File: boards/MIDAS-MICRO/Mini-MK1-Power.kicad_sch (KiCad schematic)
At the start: 20 parts, among them J201 TestPoint, J202 Conn_01x02, U201 TVS1800DRV, U202 TVS1800DRV, U203 TPS2121, U204 TPS746-Q1

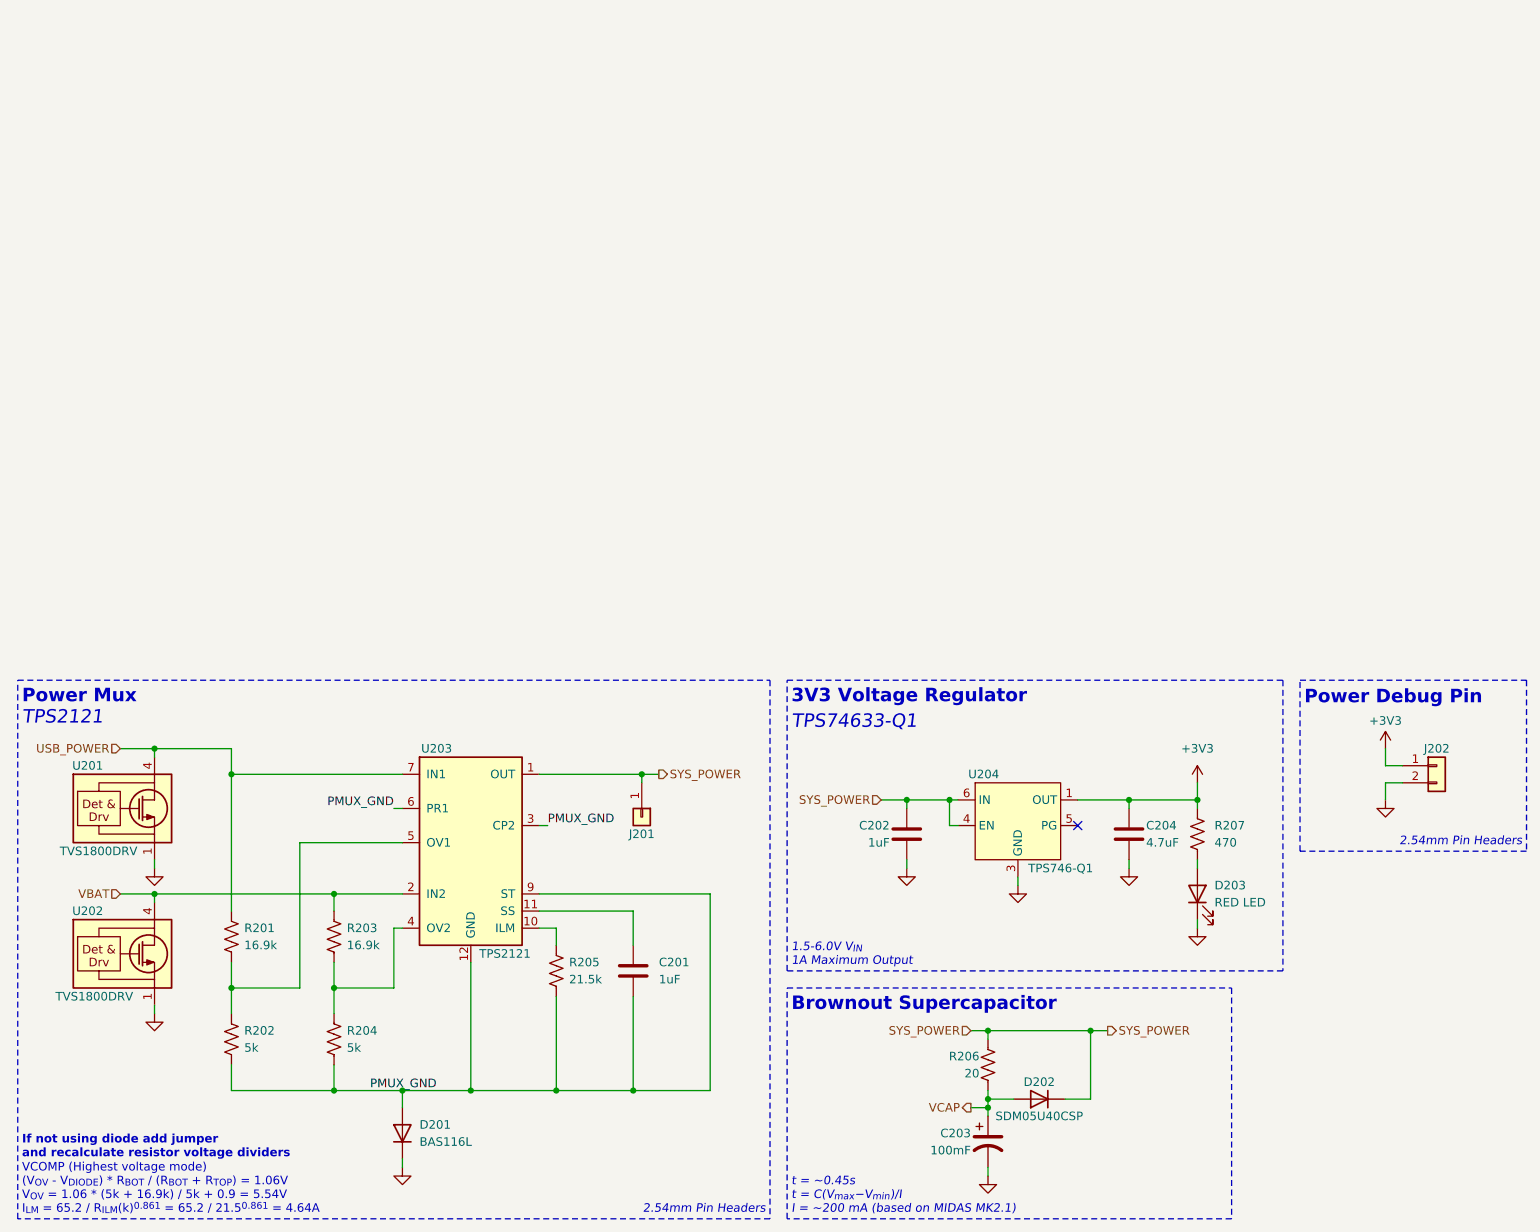
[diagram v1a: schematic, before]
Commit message: Connected I2C and SPI connection to STM32, removed power mux and supercapacitor
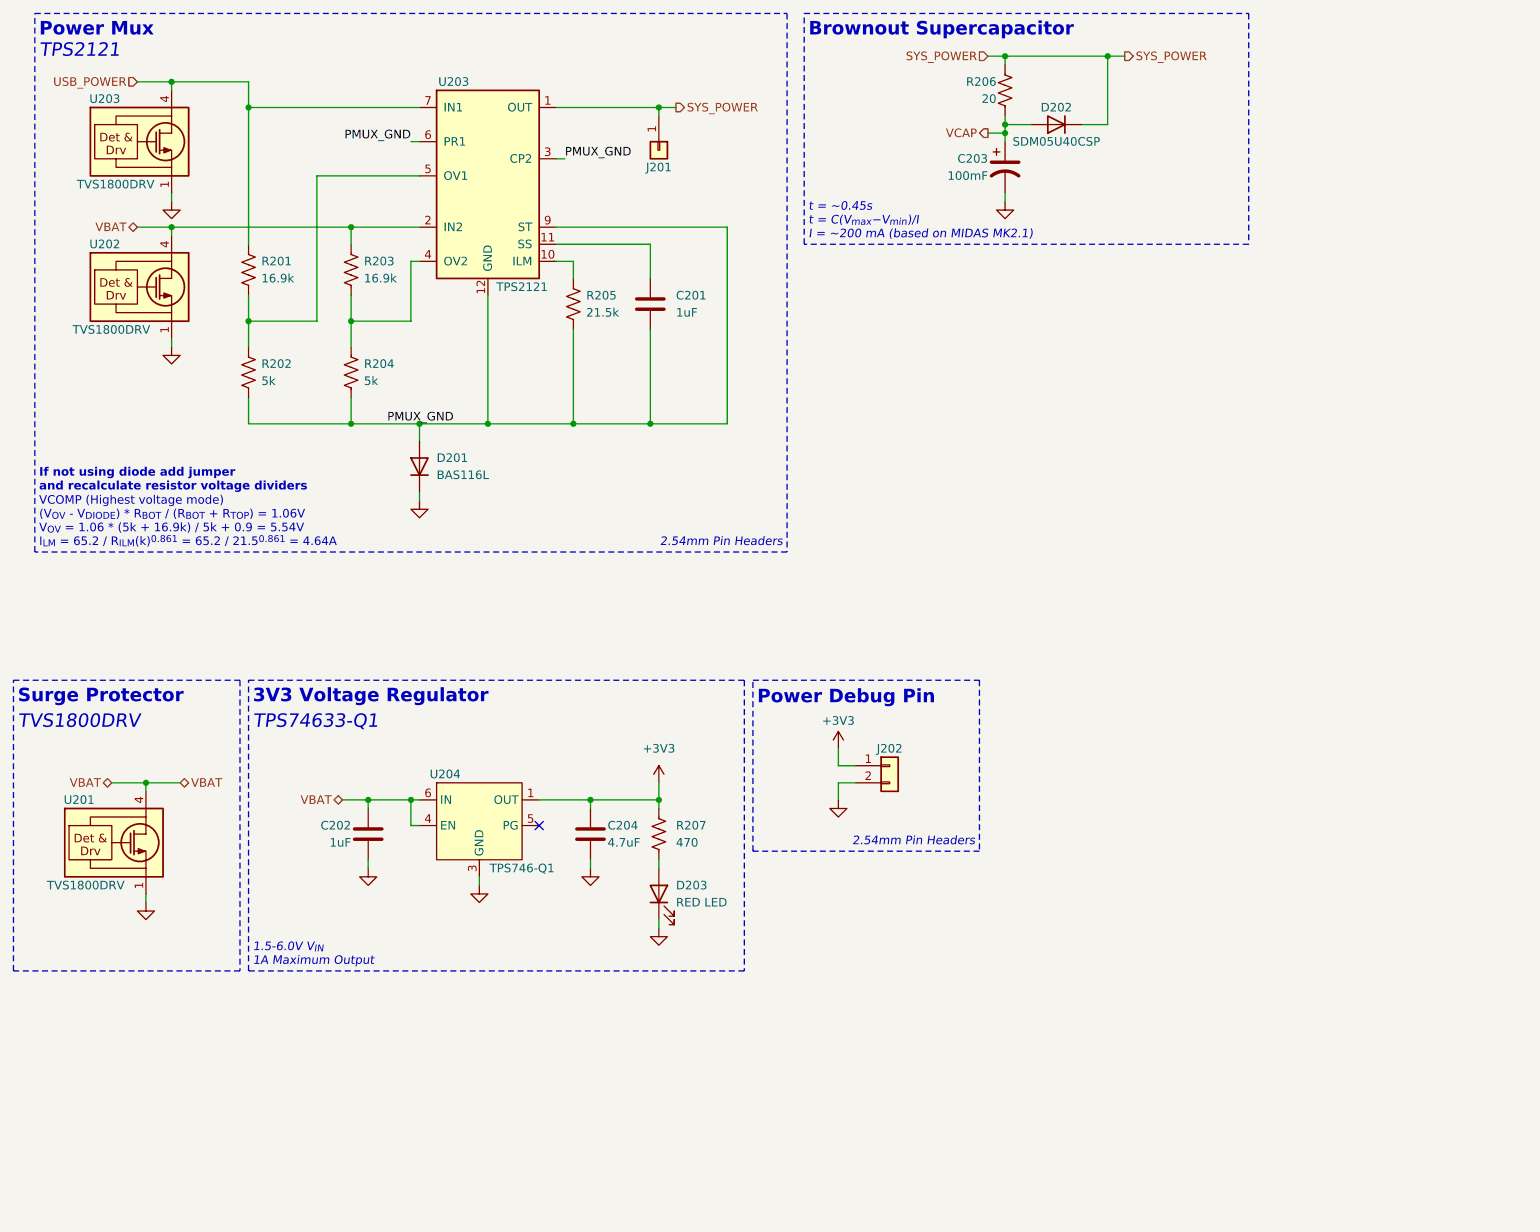
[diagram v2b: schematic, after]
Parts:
- added U201: TVS1800DRV, Package_SON:WSON-6-1EP_2x2mm_P0.65mm_EP1x1.6mm, symbol Power_Protection:TVS1800DRV
- renumbered U201 to U203
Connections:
- net EP: now also U201.1 (GND), U201.2 (GND), U201.3 (GND), U201.7 (GND)
- net SYS_POWER: no longer C202.1, U204.4 (EN), U204.6 (IN)
- net VBAT: now also C202.1, U204.4 (EN), U204.6 (IN), U201.4 (IN), U201.5 (IN), U201.6 (IN)
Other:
- note added: "Surge Protector"
- note added: "TVS1800DRV"
- title: MIDAS Mini Power Circuitry MK1 -> MIDAS Micro Power Circuitry MK1
- moved on the sheet: C201, C202, C203, C204, D201, D202, D203, J201, J202, R201, R202, R203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

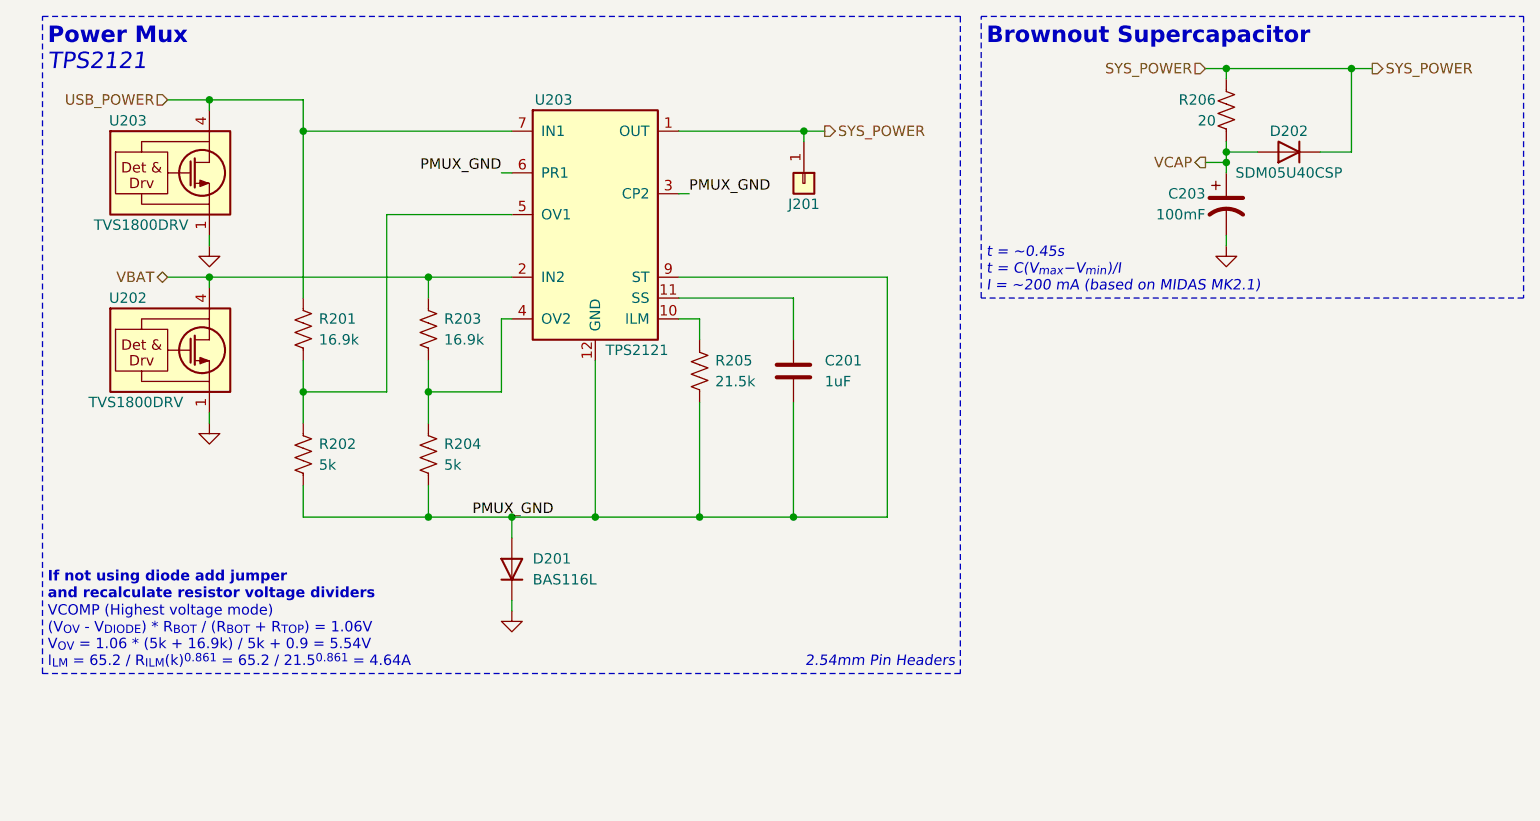
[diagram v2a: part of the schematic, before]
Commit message: Deleted unnecessary power components
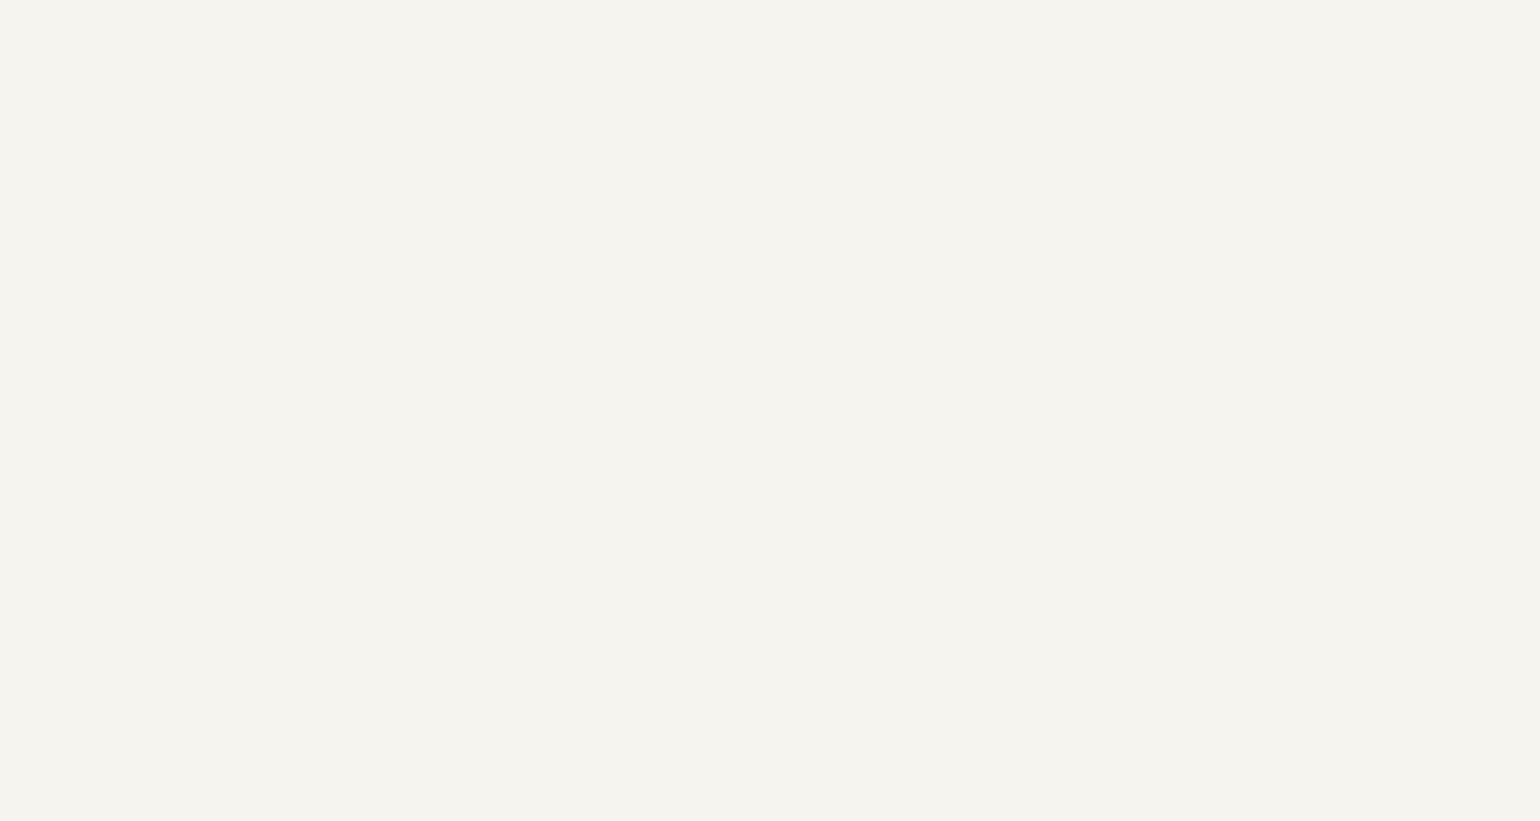
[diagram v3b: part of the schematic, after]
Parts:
- removed C201: 1uF, Capacitor_SMD:C_0402_1005Metric, symbol Device:C
- removed C203: 100mF, Capacitor_SMD:CP_Elec_10x10.5, symbol Device:C_Polarized_US
- removed D201: BAS116L, Diode_SMD:D_SOD-882, symbol Device:D
- removed D202: SDM05U40CSP, Diode_SMD:D_SOD-882, symbol Device:D
- removed J201: TestPoint, TestPoint:TestPoint_THTPad_1.5x1.5mm_Drill0.7mm, symbol Connector_Generic:Conn_01x01
- removed R201, R203: 16.9k, Resistor_SMD:R_0402_1005Metric, symbol Device:R_US
- removed R202, R204: 5k, Resistor_SMD:R_0402_1005Metric, symbol Device:R_US
- removed R205: 21.5k, Resistor_SMD:R_0402_1005Metric, symbol Device:R_US
- removed R206: 20, Resistor_SMD:R_0612_1632Metric, symbol Device:R_US
- removed U202, U203: TVS1800DRV, Package_SON:WSON-6-1EP_2x2mm_P0.65mm_EP1x1.6mm, symbol Power_Protection:TVS1800DRV
- removed U203: TPS2121, Package_DFN_QFN:Texas_VQFN-HR-12_2x2.5mm_P0.5mm, symbol Power_MUX:TPS2121
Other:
- note removed: "Brownout Supercapacitor"
- note removed: "If not using diode add jumper and recalculate resistor voltage dividers"
- note removed: "Power Mux"
- note removed: "TPS2121"
- note removed: "VCOMP (Highest voltage mode) (V_{OV} - V_{DIODE}) * R_{BOT} / (R_{BOT} + R_{TOP}) = 1.06V V_{OV} = 1.06 * (5k + 16.9k) / 5k + 0.9 = 5.54V I_{LM} = 65.2 / R_{ILM}(k)^{0.861} = 65.2 / 21.5^{0.861} = 4.64A"
- note removed: "t = ~0.45s t = C(V_{max}−V_{min})/I I = ~200 mA (based on MIDAS MK2.1)"
